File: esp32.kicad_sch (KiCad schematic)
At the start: 6 parts, among them J1 Conn_01x06, U1 ESP32-S3-WROOM-1

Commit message: final design
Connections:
- net LED_1: now also U1.21 (IO13); no longer U1.18 (IO10)
- net LED_2: now also U1.20 (IO12); no longer U1.19 (IO11)
- net LED_3: now also U1.19 (IO11); no longer U1.20 (IO12)
- net LED_4: now also U1.18 (IO10); no longer U1.21 (IO13)
- net V3.3: now also J1.3 (Pin_3); no longer J1.6 (Pin_6)
- net at J1.2 (Pin_2): now also C3.1, R1.2, U1.3 (EN); no longer U1.36 (RXD0)
- net at U1.37 (TXD0): now also J1.5 (Pin_5); no longer J1.3 (Pin_3)
- net at J1.4 (Pin_4): now also U1.36 (RXD0); no longer U1.27 (IO0)
- new net: J1.6 (Pin_6), U1.27 (IO0)
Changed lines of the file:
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@@
 	(wire
 		(pts
-			(xy 191.77 76.2) (xy 181.61 76.2)
+			(xy 191.77 76.2) (xy 186.69 76.2)
+		)
+		(stroke
+			(width 0)
+			(type default)
+		)
+	)
+	(wire
+		(pts
+			(xy 185.42 69.85) (xy 121.92 69.85)
 		)
 		(stroke
@@
 	(wire
 		(pts
-			(xy 121.92 71.12) (xy 121.92 81.28)
+			(xy 121.92 69.85) (xy 121.92 81.28)
 		)
 		(stroke
@@
 	(wire
 		(pts
-			(xy 191.77 68.58) (xy 186.69 68.58)
-		)
-		(stroke
-			(width 0)
-			(type default)
-		)
-	)
-	(wire
-		(pts
 			(xy 123.19 86.36) (xy 132.08 86.36)
 		)
@@
 	(wire
 		(pts
-			(xy 162.56 83.82) (xy 182.88 83.82)
+			(xy 171.45 71.12) (xy 171.45 81.28)
 		)
 		(stroke
@@
 	(wire
 		(pts
-			(xy 123.19 73.66) (xy 123.19 86.36)
-		)
-		(stroke
-			(width 0)
-			(type default)
-		)
-	)
-	(wire
-		(pts
-			(xy 182.88 78.74) (xy 191.77 78.74)
-		)
-		(stroke
-			(width 0)
-			(type default)
-		)
-	)
-	(wire
-		(pts
-			(xy 181.61 76.2) (xy 181.61 81.28)
+			(xy 123.19 68.58) (xy 191.77 68.58)
+		)
+		(stroke
+			(width 0)
+			(type default)
+		)
+	)
+	(wire
+		(pts
+			(xy 123.19 68.58) (xy 123.19 86.36)
+		)
+		(stroke
+			(width 0)
+			(type default)
+		)
+	)
+	(wire
+		(pts
+			(xy 172.72 73.66) (xy 172.72 83.82)
 		)
 		(stroke
@@
 	(wire
 		(pts
+			(xy 191.77 78.74) (xy 185.42 78.74)
+		)
+		(stroke
+			(width 0)
+			(type default)
+		)
+	)
+	(wire
+		(pts
+			(xy 185.42 78.74) (xy 185.42 69.85)
+		)
+		(stroke
+			(width 0)
+			(type default)
+		)
+	)
+	(wire
+		(pts
 			(xy 102.87 81.28) (xy 121.92 81.28)
 		)
@@
 	(wire
 		(pts
-			(xy 191.77 73.66) (xy 123.19 73.66)
+			(xy 191.77 73.66) (xy 172.72 73.66)
 		)
 		(stroke
@@
 	(wire
 		(pts
+			(xy 171.45 81.28) (xy 162.56 81.28)
+		)
+		(stroke
+			(width 0)
+			(type default)
+		)
+	)
+	(wire
+		(pts
 			(xy 119.38 58.42) (xy 123.19 58.42)
 		)
@@
 	(wire
 		(pts
+			(xy 191.77 71.12) (xy 171.45 71.12)
+		)
+		(stroke
+			(width 0)
+			(type default)
+		)
+	)
+	(wire
+		(pts
 			(xy 191.77 81.28) (xy 189.23 81.28)
 		)
@@
 	(wire
 		(pts
-			(xy 182.88 83.82) (xy 182.88 78.74)
-		)
-		(stroke
-			(width 0)
-			(type default)
-		)
-	)
-	(wire
-		(pts
 			(xy 123.19 50.8) (xy 127 50.8)
 		)
@@
 	(wire
 		(pts
-			(xy 191.77 71.12) (xy 121.92 71.12)
+			(xy 172.72 83.82) (xy 162.56 83.82)
 		)
 		(stroke
@@
 	(wire
 		(pts
-			(xy 181.61 81.28) (xy 162.56 81.28)
-		)
-		(stroke
-			(width 0)
-			(type default)
-		)
-	)
-	(wire
-		(pts
 			(xy 123.19 58.42) (xy 123.19 60.96)
 		)
@@
 	(wire
 		(pts
-			(xy 186.69 68.58) (xy 186.69 63.5)
-		)
-		(stroke
-			(width 0)
-			(type default)
+			(xy 186.69 60.96) (xy 186.69 76.2)
+		)
+		(stroke
+			(width 0)
+			(type default)
+		)
+	)
+	(hierarchical_label "GND"
+		(shape passive)
+		(at 147.32 137.16 270)
+		(effects
+			(font
+				(size 1.27 1.27)
+			)
+			(justify right)
+		)
+	)
+	(hierarchical_label "GND"
+		(shape passive)
+		(at 100.33 88.9 270)
+		(effects
+			(font
+				(size 1.27 1.27)
+			)
+			(justify right)
 		)
 	)
 	(hierarchical_label "LED_4"
 		(shape bidirectional)
+		(at 118.11 111.76 180)
+		(effects
+			(font
+				(size 1.27 1.27)
+			)
+			(justify right)
+		)
+	)
+	(hierarchical_label "V3.3"
+		(shape passive)
+		(at 123.19 48.26 90)
+		(effects
+			(font
+				(size 1.27 1.27)
+			)
+			(justify left)
+		)
+	)
+	(hierarchical_label "GND"
+		(shape passive)
+		(at 123.19 60.96 270)
+		(effects
+			(font
+				(size 1.27 1.27)
+			)
+			(justify right)
+		)
+	)
+	(hierarchical_label "LED_2"
+		(shape bidirectional)
+		(at 118.11 116.84 180)
+		(effects
+			(font
+				(size 1.27 1.27)
+			)
+			(justify right)
+		)
+	)
+	(hierarchical_label "V3.3"
+		(shape passive)
+		(at 102.87 73.66 90)
+		(effects
+			(font
+				(size 1.27 1.27)
+			)
+			(justify left)
+		)
+	)
+	(hierarchical_label "LED_1"
+		(shape bidirectional)
 		(at 118.11 119.38 180)
 		(effects
@@
 	(hierarchical_label "GND"
 		(shape passive)
-		(at 147.32 137.16 270)
-		(effects
-			(font
-				(size 1.27 1.27)
-			)
-			(justify right)
-		)
-	)
-	(hierarchical_label "GND"
-		(shape passive)
-		(at 100.33 88.9 270)
+		(at 189.23 82.55 270)
 		(effects
 			(font
@@
 	(hierarchical_label "V3.3"
 		(shape passive)
-		(at 123.19 48.26 90)
+		(at 186.69 60.96 90)
 		(effects
 			(font
@@
 		)
 	)
-	(hierarchical_label "GND"
-		(shape passive)
-		(at 123.19 60.96 270)
-		(effects
-			(font
-				(size 1.27 1.27)
-			)
-			(justify right)
+	(hierarchical_label "V3.3"
+		(shape passive)
+		(at 147.32 57.15 90)
+		(effects
+			(font
+				(size 1.27 1.27)
+			)
+			(justify left)
 		)
 	)
 	(hierarchical_label "LED_3"
 		(shape bidirectional)
-		(at 118.11 116.84 180)
-		(effects
-			(font
-				(size 1.27 1.27)
-			)
-			(justify right)
-		)
-	)
-	(hierarchical_label "V3.3"
-		(shape passive)
-		(at 102.87 73.66 90)
-		(effects
-			(font
-				(size 1.27 1.27)
-			)
-			(justify left)
-		)
-	)
-	(hierarchical_label "GND"
-		(shape passive)
-		(at 189.23 82.55 270)
-		(effects
-			(font
-				(size 1.27 1.27)
-			)
-			(justify right)
-		)
-	)
-	(hierarchical_label "V3.3"
-		(shape passive)
-		(at 186.69 63.5 90)
-		(effects
-			(font
-				(size 1.27 1.27)
-			)
-			(justify left)
-		)
-	)
-	(hierarchical_label "V3.3"
-		(shape passive)
-		(at 147.32 57.15 90)
-		(effects
-			(font
-				(size 1.27 1.27)
-			)
-			(justify left)
-		)
-	)
-	(hierarchical_label "LED_2"
-		(shape bidirectional)
 		(at 118.11 114.3 180)
 		(effects
 			(font
-				(size 1.27 1.27)
-			)
-			(justify right)
-		)
-	)
-	(hierarchical_label "LED_1"
-		(shape bidirectional)
-		(at 118.11 111.76 180)
-		(effects
-			(font

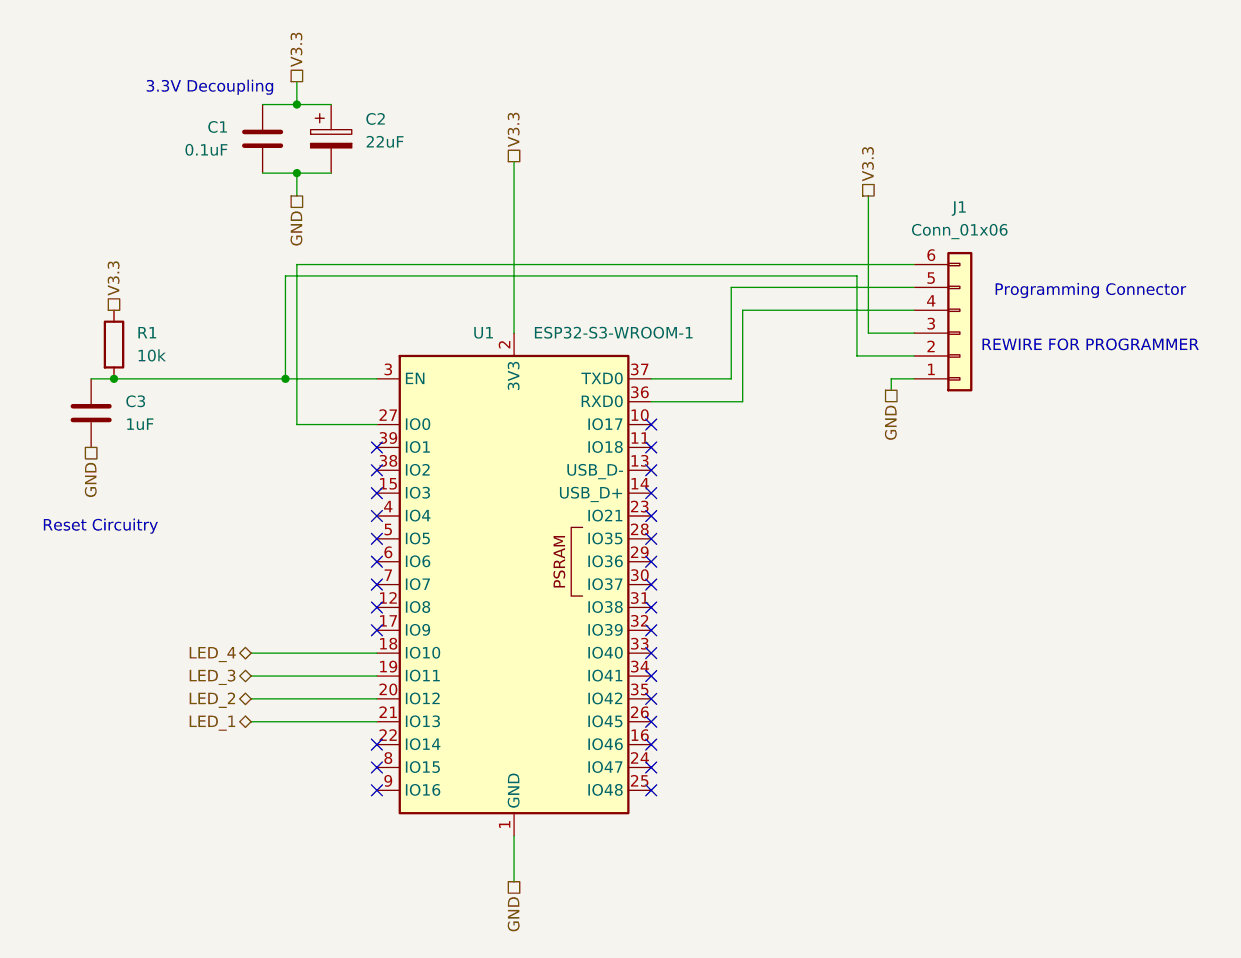
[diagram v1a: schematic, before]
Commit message: all one layer added usb
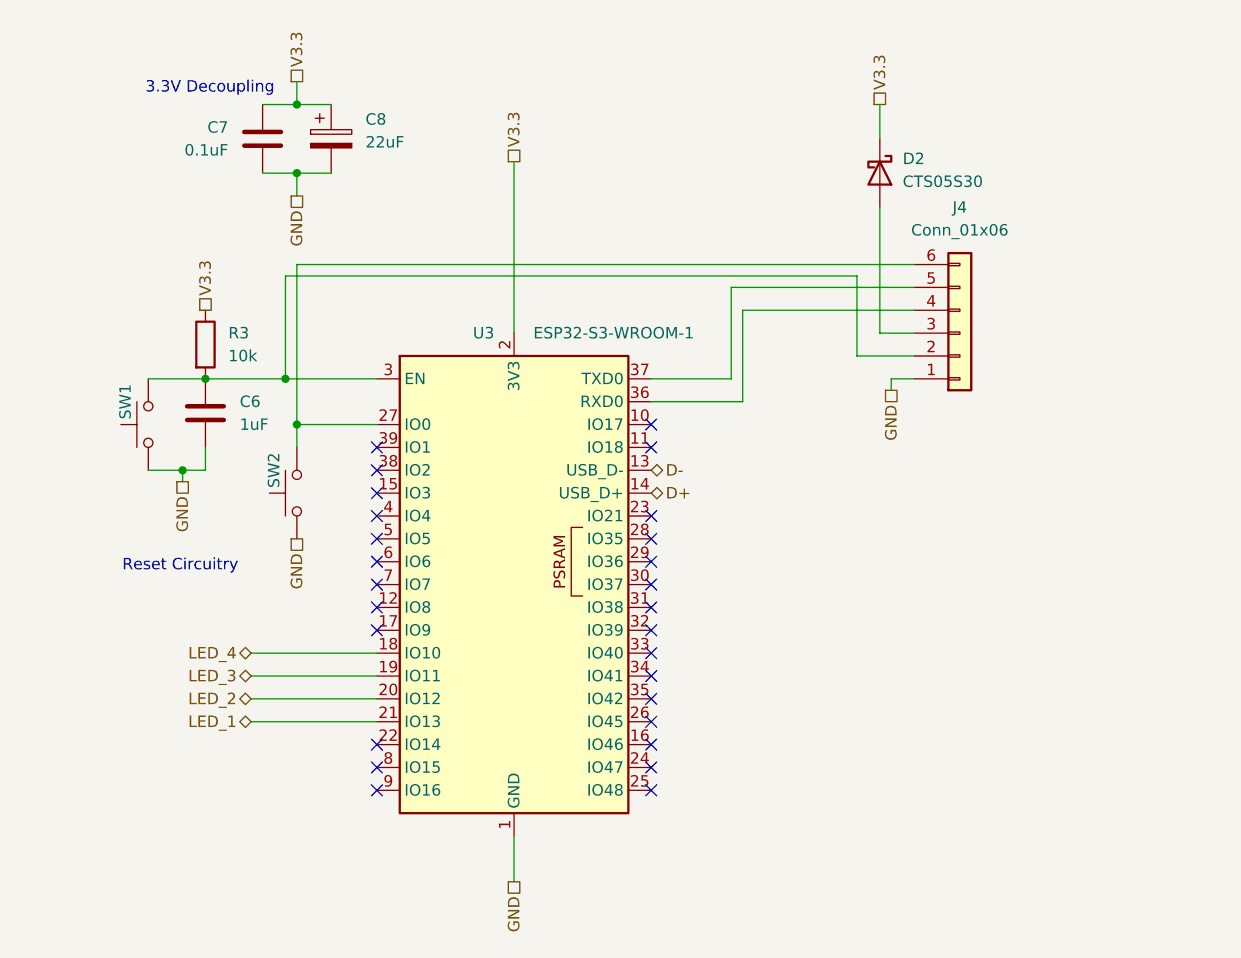
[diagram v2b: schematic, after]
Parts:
- added D2: CTS05S30, Diode_SMD:D_0805_2012Metric, symbol Diode:B220
- added SW1, SW2: SW_Push, Button_Switch_SMD:SW_Push_1P1T_XKB_TS-1187A, symbol Switch:SW_Push
- C6: renamed from C3; footprint Capacitor_SMD:C_0402_1005Metric_Pad0.74x0.62mm_HandSolder -> Capacitor_SMD:C_0402_1005Metric
- C7: renamed from C1; footprint Capacitor_SMD:C_0402_1005Metric_Pad0.74x0.62mm_HandSolder -> Capacitor_SMD:C_0402_1005Metric
- renumbered C2 to C8, J1 to J4, R1 to R3, U1 to U3
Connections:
- net GND: now also SW1.1, SW2.1
- net V3.3: now also D2.1 (K); no longer J4.3 (Pin_3)
- net at C6.1, J4.2 (Pin_2), R3.2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: now also SW1.2
- net at J4.6 (Pin_6), U3.27 (IO0): now also SW2.2
- net D-: now reaches U3.13 (USB_D-)
- net D+: now reaches U3.14 (USB_D+)
- new net: D2.2 (A), J4.3 (Pin_3)
- no-connect marks 29 -> 27
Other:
- note removed: "Programming Connector REWIRE FOR PROGRAMMER"
- moved on the sheet: C6, R3

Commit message: rev 2
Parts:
- removed D2: CTS05S30, Diode_SMD:D_0805_2012Metric, symbol Diode:B220
- removed J4: Conn_01x06, Connector_PinHeader_2.54mm:PinHeader_1x06_P2.54mm_Vertical, symbol Connector_Generic:Conn_01x06
- R3: footprint Resistor_SMD:R_0402_1005Metric_Pad0.72x0.64mm_HandSolder -> Resistor_SMD:R_0402_1005
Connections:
- net GND: now also U3.26 (IO45)
- net RELAY: now reaches U3.9 (IO16)
- no-connect marks 27 -> 25
